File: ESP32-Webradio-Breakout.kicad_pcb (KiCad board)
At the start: 2 copper layers, 68 x 31 mm, 53 parts, among them J1 AudioJack3, J2 Conn_01x01, J3 Conn_01x02, P1 USB_C_Plug, Q1 BC817, Q2 BC817, Q3 BC817, SW1 RotaryEncoder_Switch, U1 AMS1117-3.3, U2 ESP32-WROOM-32, U3 CH340C, U4 PCF8574TS, U5 DS18B20

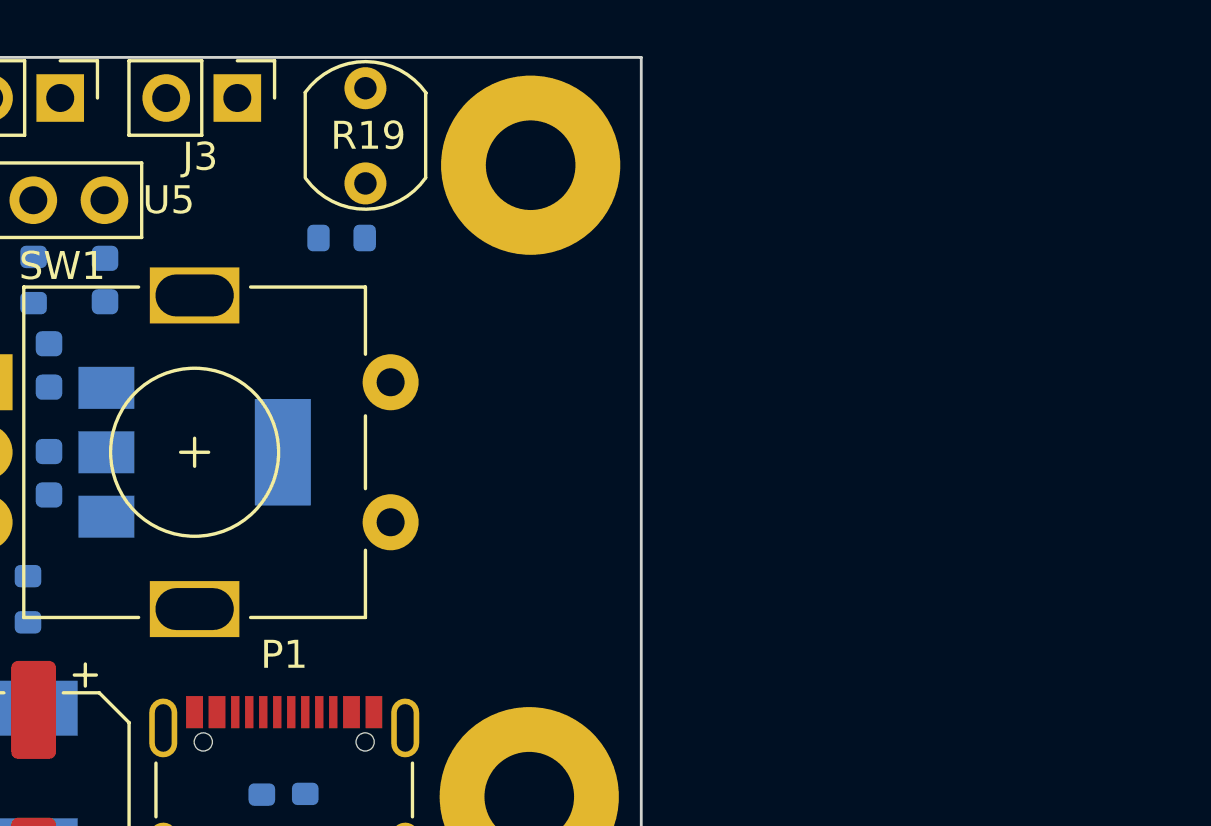
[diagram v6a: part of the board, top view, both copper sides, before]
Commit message: Added MicroSD cardreader
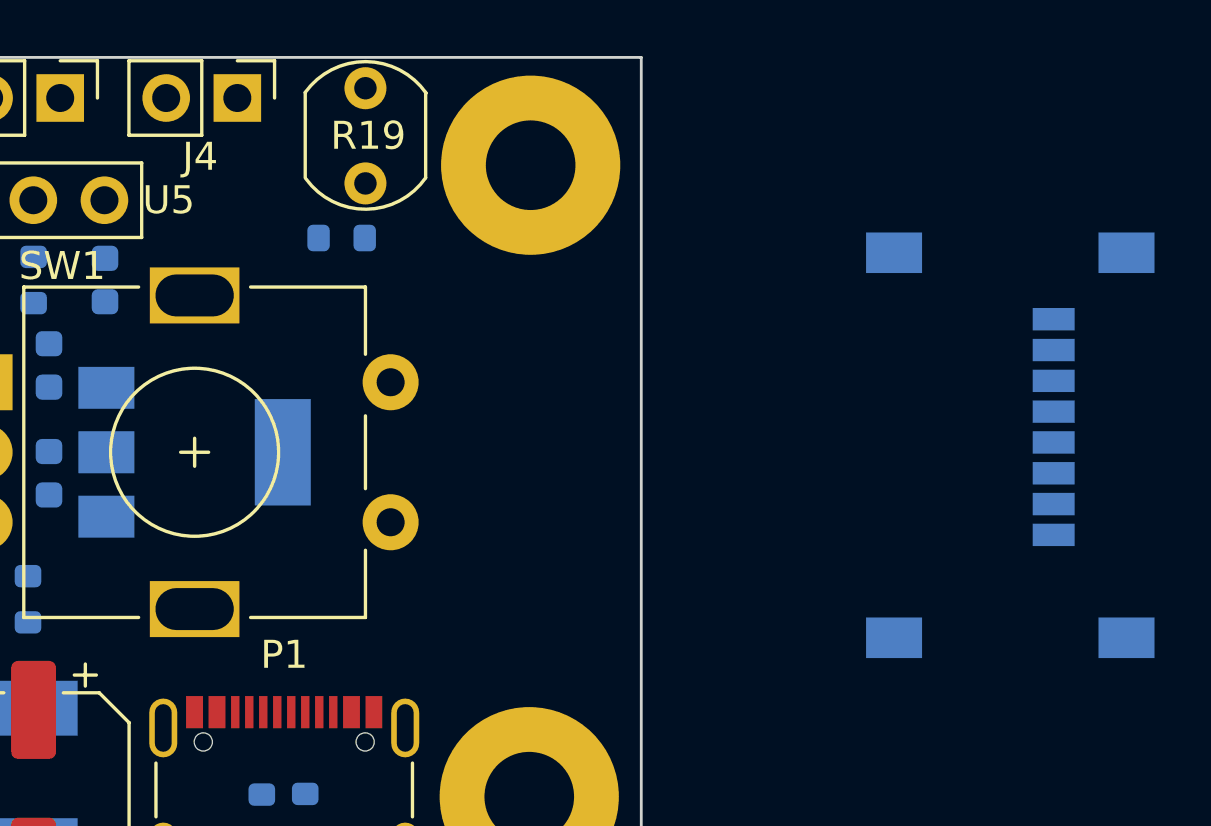
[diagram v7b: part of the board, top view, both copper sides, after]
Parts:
- added J3: Micro_SD_Card, Connector_Card:microSD_HC_Wuerth_693072010801, B.Cu at (106.2, 38.9)
- renumbered J3 to J4
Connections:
- U2 pad 13: unconnected-(U2-Pad13) -> /SD_CLK
- U2 pad 14: unconnected-(U2-Pad14) -> /SD_D2
- U2 pad 16: unconnected-(U2-Pad16) -> /SD_D3
- U2 pad 23: unconnected-(U2-Pad23) -> /SD_CMD
- U2 pad 24: unconnected-(U2-Pad24) -> /SD_D0
- U2 pad 26: /Touch_Sens -> /SD_D1
- U2 pad 37: unconnected-(U2-Pad37) -> /Touch_Sens
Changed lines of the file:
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@@
   (net 49 "unconnected-(U2-Pad4)")
   (net 50 "unconnected-(U2-Pad5)")
-  (net 51 "unconnected-(U2-Pad13)")
-  (net 52 "unconnected-(U2-Pad14)")
-  (net 53 "unconnected-(U2-Pad16)")
+  (net 51 "/SD_D2")
+  (net 52 "/SD_D3")
+  (net 53 "/SD_CMD")
   (net 54 "unconnected-(U2-Pad17)")
   (net 55 "unconnected-(U2-Pad18)")
@@
   (net 58 "unconnected-(U2-Pad21)")
   (net 59 "unconnected-(U2-Pad22)")
-  (net 60 "unconnected-(U2-Pad23)")
-  (net 61 "unconnected-(U2-Pad24)")
+  (net 60 "/SD_CLK")
+  (net 61 "/SD_D0")
   (net 62 "/Touch_Sens")
   (net 63 "unconnected-(U2-Pad27)")
@@
   (net 68 "/RXD")
   (net 69 "/TXD")
-  (net 70 "unconnected-(U2-Pad37)")
+  (net 70 "/SD_D1")
   (net 71 "unconnected-(U3-Pad7)")
   (net 72 "unconnected-(U3-Pad8)")
@@
     (property "Sheetname" "")
     (attr through_hole)
-    (fp_text reference "J3" (at 2.1 1.325) (layer "F.SilkS")
+    (fp_text reference "J4" (at 2.1 1.325) (layer "F.SilkS")
       (effects (font (size 1 1) (thickness 0.15)))
     )
@@
       (net 48 "/LCD_Dimm") (pinfunction "IO27") (pintype "bidirectional"))
     (pad "13" smd rect locked (at -8.5 6.985 180) (size 2 0.9) (layers "F.Cu" "F.Paste" "F.Mask")
-      (net 51 "unconnected-(U2-Pad13)") (pinfunction "IO14") (pintype "bidirectional+no_connect"))
+      (net 60 "/SD_CLK") (pinfunction "IO14") (pintype "bidirectional"))
     (pad "14" smd rect locked (at -8.5 8.255 180) (size 2 0.9) (layers "F.Cu" "F.Paste" "F.Mask")
-      (net 52 "unconnected-(U2-Pad14)") (pinfunction "IO12") (pintype "bidirectional+no_connect"))
+      (net 51 "/SD_D2") (pinfunction "IO12") (pintype "bidirectional"))
     (pad "15" smd rect locked (at -5.715 9.255 270) (size 2 0.9) (layers "F.Cu" "F.Paste" "F.Mask")
       (net 2 "GND") (pinfunction "GND") (pintype "passive"))
     (pad "16" smd rect locked (at -4.445 9.255 270) (size 2 0.9) (layers "F.Cu" "F.Paste" "F.Mask")
-      (net 53 "unconnected-(U2-Pad16)") (pinfunction "IO13") (pintype "bidirectional+no_connect"))
+      (net 52 "/SD_D3") (pinfunction "IO13") (pintype "bidirectional"))
     (pad "17" smd rect locked (at -3.175 9.255 270) (size 2 0.9) (layers "F.Cu" "F.Paste" "F.Mask")
       (net 54 "unconnected-(U2-Pad17)") (pinfunction "SHD/SD2") (pintype "bidirectional+no_connect"))
@@
       (net 59 "unconnected-(U2-Pad22)") (pinfunction "SDI/SD1") (pintype "bidirectional+no_connect"))
     (pad "23" smd rect locked (at 4.445 9.255 270) (size 2 0.9) (layers "F.Cu" "F.Paste" "F.Mask")
-      (net 60 "unconnected-(U2-Pad23)") (pinfunction "IO15") (pintype "bidirectional+no_connect"))
+      (net 53 "/SD_CMD") (pinfunction "IO15") (pintype "bidirectional"))
     (pad "24" smd rect locked (at 5.715 9.255 270) (size 2 0.9) (layers "F.Cu" "F.Paste" "F.Mask")
-      (net 61 "unconnected-(U2-Pad24)") (pinfunction "IO2") (pintype "bidirectional+no_connect"))
+      (net 61 "/SD_D0") (pinfunction "IO2") (pintype "bidirectional"))
     (pad "25" smd rect locked (at 8.5 8.255 180) (size 2 0.9) (layers "F.Cu" "F.Paste" "F.Mask")
       (net 36 "/IO0") (pinfunction "IO0") (pintype "bidirectional"))
     (pad "26" smd rect locked (at 8.5 6.985 180) (size 2 0.9) (layers "F.Cu" "F.Paste" "F.Mask")
-      (net 62 "/Touch_Sens") (pinfunction "IO4") (pintype "bidirectional"))
+      (net 70 "/SD_D1") (pinfunction "IO4") (pintype "bidirectional"))
     (pad "27" smd rect locked (at 8.5 5.715 180) (size 2 0.9) (layers "F.Cu" "F.Paste" "F.Mask")
       (net 63 "unconnected-(U2-Pad27)") (pinfunction "IO16") (pintype "bidirectional+no_connect"))
@@
       (net 25 "/SCL") (pinfunction "IO22") (pintype "bidirectional"))
     (pad "37" smd rect locked (at 8.5 -6.985 180) (size 2 0.9) (layers "F.Cu" "F.Paste" "F.Mask")
-      (net 70 "unconnected-(U2-Pad37)") (pinfunction "IO23") (pintype "bidirectional+no_connect"))
+      (net 62 "/Touch_Sens") (pinfunction "IO23") (pintype "bidirectional"))
     (pad "38" smd rect locked (at 8.5 -8.255 180) (size 2 0.9) (layers "F.Cu" "F.Paste" "F.Mask")
       (net 2 "GND") (pinfunction "GND") (pintype "passive"))
@@
       (offset (xyz 0 0 0))
       (scale (xyz 1 1 1))
+      (rotate (xyz 0 0 0))
+    )
+  )
+  (footprint "Connector_Card:microSD_HC_Wuerth_693072010801" (layer "B.Cu")
+    (at 106.1775 38.85 90)
+    (descr "http://katalog.we-online.de/em/datasheet/693072010801.pdf")
+    (tags "Micro SD Wuerth Wurth Würth")
+    (property "Sheetfile" "ESP32-Webradio-Breakout.kicad_sch")
+    (property "Sheetname" "")
+    (attr smd)
+    (fp_text reference "J3" (at 0 7.99 90) (layer "B.SilkS")
+      (effects (font (size 1 1) (thickness 0.15)) (justify mirror))
+    )
+    (fp_text value "Micro_SD_Card" (at 0 -9.22 90) (layer "B.Fab")
+      (effects (font (size 1 1) (thickness 0.15)) (justify mirror))
+    )
+    (fp_text user "${REFERENCE}" (at 0 -1.15 90) (layer "B.Fab")
+      (effects (font (size 1 1) (thickness 0.15)) (justify mirror))
+    )
+    (fp_line (start -5.5 5.81) (end -5.5 6.81) (layer "B.SilkS") (width 0.12))
+    (fp_line (start 6.91 -8.11) (end -6.91 -8.11) (layer "B.SilkS") (width 0.12))
+    (fp_line (start -3 6.21) (end -2.2 6.11) (layer "B.SilkS") (width 0.12))
+    (fp_line (start -5.5 6.71) (end -4.7 6.51) (layer "B.SilkS") (width 0.12))
+    (fp_line (start 3.7 6.31) (end 5 6.61) (layer "B.SilkS") (width 0.12))
+    (fp_line (start -4.7 6.51) (end -3 6.21) (layer "B.SilkS") (width 0.12))
+    (fp_line (start 0.9 6.01) (end 2.2 6.11) (layer "B.SilkS") (width 0.12))
+    (fp_line (start -0.9 6.01) (end 0.9 6.01) (layer "B.SilkS") (width 0.12))
+    (fp_line (start 6.91 -5.41) (end 6.91 -8.11) (layer "B.SilkS") (width 0.12))
+    (fp_line (start 2.2 6.11) (end 3.7 6.31) (layer "B.SilkS") (width 0.12))
+    (fp_line (start -6.91 5.81) (end 6.91 5.81) (layer "B.SilkS") (width 0.12))
+    (fp_line (start -5 7.31) (end 5 7.31) (layer "B.SilkS") (width 0.12))
+    (fp_line (start -6.91 -5.41) (end -6.91 -8.11) (layer "B.SilkS") (width 0.12))
+    (fp_line (start -6.91 5.81) (end -6.91 5.41) (layer "B.SilkS") (width 0.12))
+    (fp_line (start -6.91 2.89) (end -6.91 -2.89) (layer "B.SilkS") (width 0.12))
+    (fp_line (start 6.91 2.89) (end 6.91 -2.89) (layer "B.SilkS") (width 0.12))
+    (fp_line (start 6.91 5.81) (end 6.91 5.41) (layer "B.SilkS") (width 0.12))
+    (fp_line (start 5.5 5.81) (end 5.5 6.81) (layer "B.SilkS") (width 0.12))
+    (fp_line (start -2.2 6.11) (end -0.9 6.01) (layer "B.SilkS") (width 0.12))
+    (fp_line (start 5 6.61) (end 5.5 6.71) (layer "B.SilkS") (width 0.12))
+    (fp_arc (start 5.5 6.81) (mid 5.353553 7.163553) (end 5 7.31) (layer "B.SilkS") (width 0.12))
+    (fp_arc (start -5 7.31) (mid -5.353553 7.163553) (end -5.5 6.81) (layer "B.SilkS") (width 0.12))
+    (fp_line (start 8.08 6.2) (end 8.08 -8.5) (layer "B.CrtYd") (width 0.05))
+    (fp_line (start 8.08 -8.5) (end -8.08 -8.5) (layer "B.CrtYd") (width 0.05))
+    (fp_line (start -8.08 6.2) (end -8.08 -8.5) (layer "B.CrtYd") (width 0.05))
+    (fp_line (start 8.08 6.2) (end -8.08 6.2) (layer "B.CrtYd") (width 0.05))
+    (fp_line (start 6.8 5.7) (end -6.8 5.7) (layer "B.Fab") (width 0.1))
+    (fp_line (start 6.8 -8) (end 6.8 5.7) (layer "B.Fab") (width 0.1))
+    (fp_line (start -6.8 -8) (end 6.8 -8) (layer "B.Fab") (width 0.1))
+    (fp_line (start -6.8 5.7) (end -6.8 -8) (layer "B.Fab") (width 0.1))
+    (pad "1" smd rect (at -3.2 1.55 90) (size 0.8 1.5) (layers "B.Cu" "B.Paste" "B.Mask")
+      (net 51 "/SD_D2") (pinfunction "DAT2") (pintype "bidirectional"))
+    (pad "2" smd rect (at -2.1 1.55 90) (size 0.8 1.5) (layers "B.Cu" "B.Paste" "B.Mask")
+      (net 52 "/SD_D3") (pinfunction "DAT3/CD") (pintype "bidirectional"))
+    (pad "3" smd rect (at -1 1.55 90) (size 0.8 1.5) (layers "B.Cu" "B.Paste" "B.Mask")
+      (net 53 "/SD_CMD") (pinfunction "CMD") (pintype "input"))
+    (pad "4" smd rect (at 0.1 1.55 90) (size 0.8 1.5) (layers "B.Cu" "B.Paste" "B.Mask")
+      (net 1 "+3V3") (pinfunction "VDD") (pintype "power_in"))
+    (pad "5" smd rect (at 1.2 1.55 90) (size 0.8 1.5) (layers "B.Cu" "B.Paste" "B.Mask")
+      (net 60 "/SD_CLK") (pinfunction "CLK") (pintype "input"))
+    (pad "6" smd rect (at 2.3 1.55 90) (size 0.8 1.5) (layers "B.Cu" "B.Paste" "B.Mask")
+      (net 2 "GND") (pinfunction "VSS") (pintype "power_in"))
+    (pad "7" smd rect (at 3.4 1.55 90) (size 0.8 1.5) (layers "B.Cu" "B.Paste" "B.Mask")
+      (net 61 "/SD_D0") (pinfunction "DAT0") (pintype "bidirectional"))
+    (pad "8" smd rect (at 4.5 1.55 90) (size 0.8 1.5) (layers "B.Cu" "B.Paste" "B.Mask")
+      (net 70 "/SD_D1") (pinfunction "DAT1") (pintype "bidirectional"))
+    (pad "9" smd rect (at -6.875 4.15 90) (size 1.45 2) (layers "B.Cu" "B.Paste" "B.Mask")
+      (net 2 "GND") (pinfunction "SHIELD") (pintype "passive"))
+    (pad "9" smd rect (at 6.875 -4.15 90) (size 1.45 2) (layers "B.Cu" "B.Paste" "B.Mask")
+      (net 2 "GND") (pinfunction "SHIELD") (pintype "passive"))
+    (pad "9" smd rect (at -6.875 -4.15 90) (size 1.45 2) (layers "B.Cu" "B.Paste" "B.Mask")
+      (net 2 "GND") (pinfunction "SHIELD") (pintype "passive"))
+    (pad "9" smd rect (at 6.875 4.15 90) (size 1.45 2) (layers "B.Cu" "B.Paste" "B.Mask")
+      (net 2 "GND") (pinfunction "SHIELD") (pintype "passive"))
+    (model "${KICAD6_3DMODEL_DIR}/Connector_Card.3dshapes/microSD_HC_Wuerth_693072010801.wrl"
+      (offset (xyz 0 0 0))
+      (scale (xyz 1 1 1))

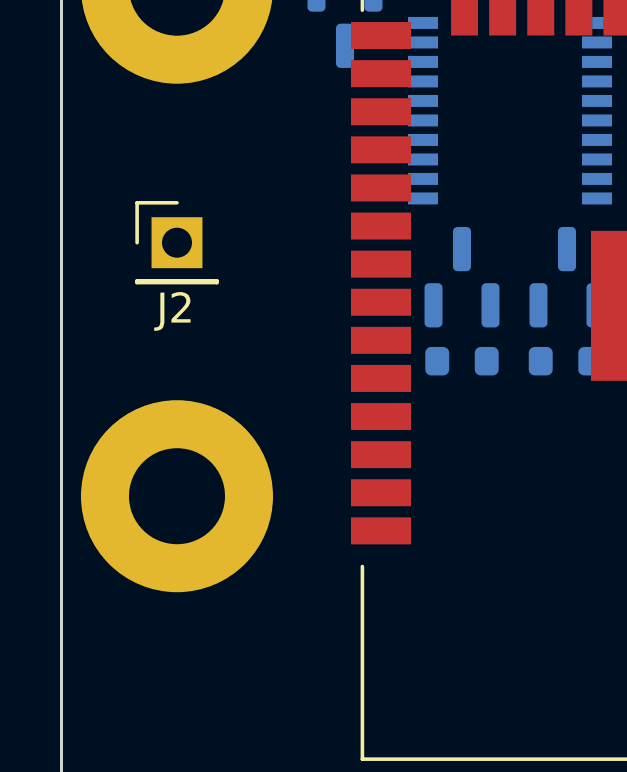
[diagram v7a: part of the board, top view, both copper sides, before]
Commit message: Moved mounting hole out of keepout zone
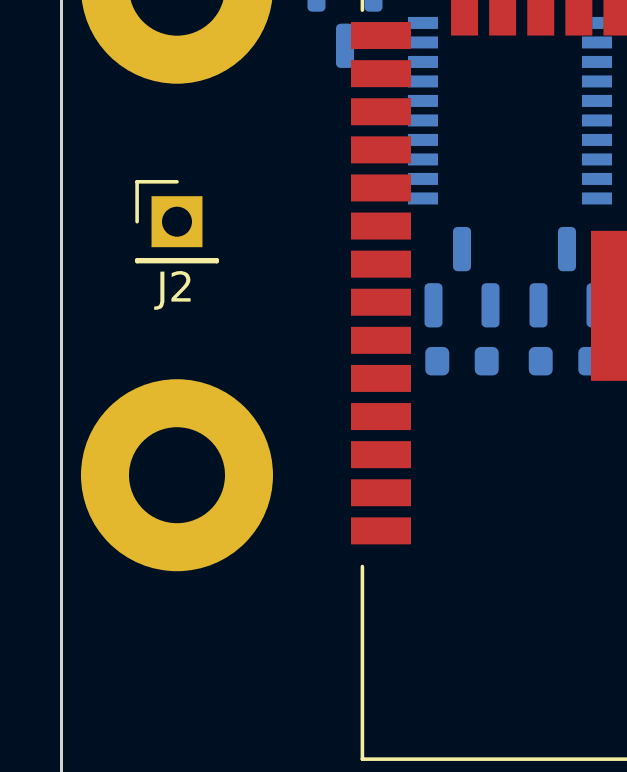
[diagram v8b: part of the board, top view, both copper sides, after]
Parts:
- moved J2 0.70 mm to (28.9, 36.6)
- moved ? 0.70 mm to (28.9, 45.1)
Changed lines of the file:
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@@
   )
   (footprint "" locked (layer "F.Cu")
-    (at 28.85 45.8)
+    (at 28.85 45.1)
     (attr board_only exclude_from_bom)
     (fp_text reference "" (at 0 0) (layer "F.SilkS")
@@
   )
   (footprint "Connector_PinHeader_2.54mm:PinHeader_1x01_P2.54mm_Vertical" locked (layer "F.Cu")
-    (at 28.85 37.35)
+    (at 28.85 36.65)
     (descr "Through hole straight pin header, 1x01, 2.54mm pitch, single row")
     (tags "Through hole pin header THT 1x01 2.54mm single row")
@@
   (gr_line locked (start 93 25) (end 93 56) (layer "Edge.Cuts") (width 0.1))
   (gr_line locked (start 25 56) (end 25 25) (layer "Edge.Cuts") (width 0.1))
-  (gr_text "TOUCH" (at 31 37.35 90) (layer "B.SilkS")
+  (gr_text "TOUCH" (at 31 36.65 90) (layer "B.SilkS")
     (effects (font (size 1 1) (thickness 0.15)) (justify mirror))
   )
